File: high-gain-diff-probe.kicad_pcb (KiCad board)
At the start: 4 copper layers, 119.5 x 74.5 mm, 107 parts, among them J1 30V DC IN, J2 BNC, J4 BNC, J5 BNC, K1 FTR-B3SA012Z, K2 FTR-B3SA012Z, Q1 MMBT3906, SW1 MB04L1NCGD, SW2 MB05L1NCGD, SW3 SPDT, SW4 MB04L1NCGD, SW6 SPDT, U1 AD8428BRZ, U2 OP1177AR, U3 BUF634A, U6 LM393, U7 AD8671, U8 BUF634A

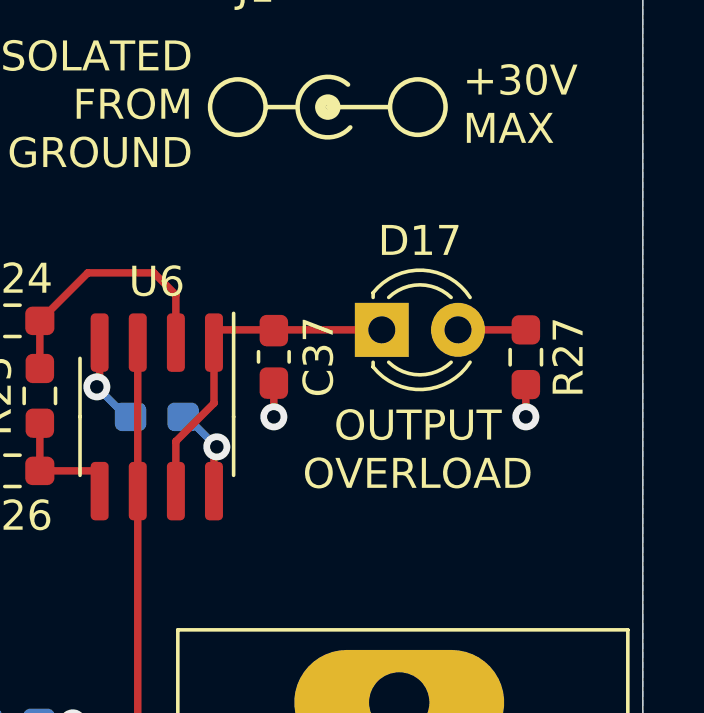
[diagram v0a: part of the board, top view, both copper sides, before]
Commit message: Add MPNs for everything else
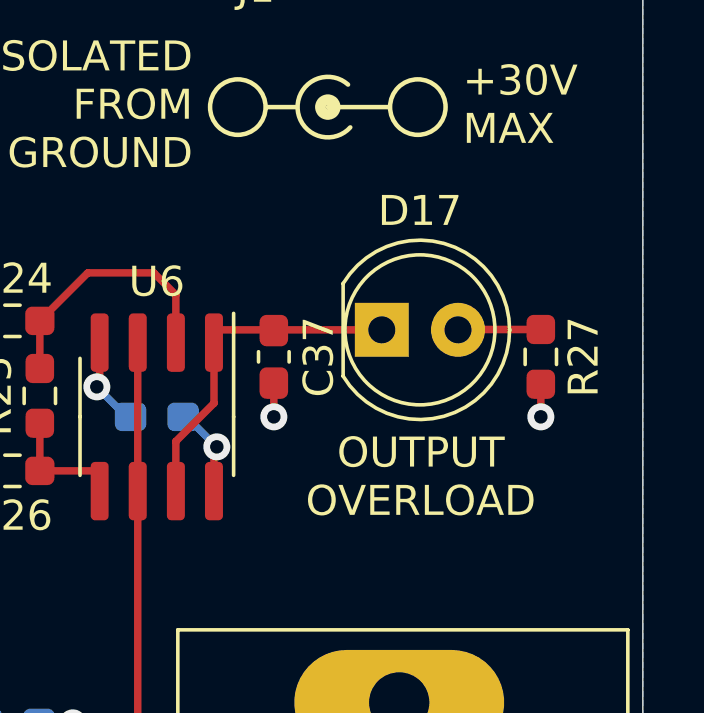
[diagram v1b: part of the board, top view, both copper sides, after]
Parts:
- D17: value LED -> RED LED; footprint LED_THT:LED_D3.0mm -> LED_THT:LED_D5.0mm
- F4: value 1A Fast -> 500mA Fast
- U2: value OP1177AR -> OP1177
- moved R27 0.50 mm to (206.1, 100.9)
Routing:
- net Net-(D17-Pad2): track 2.26 -> 2.77 mm

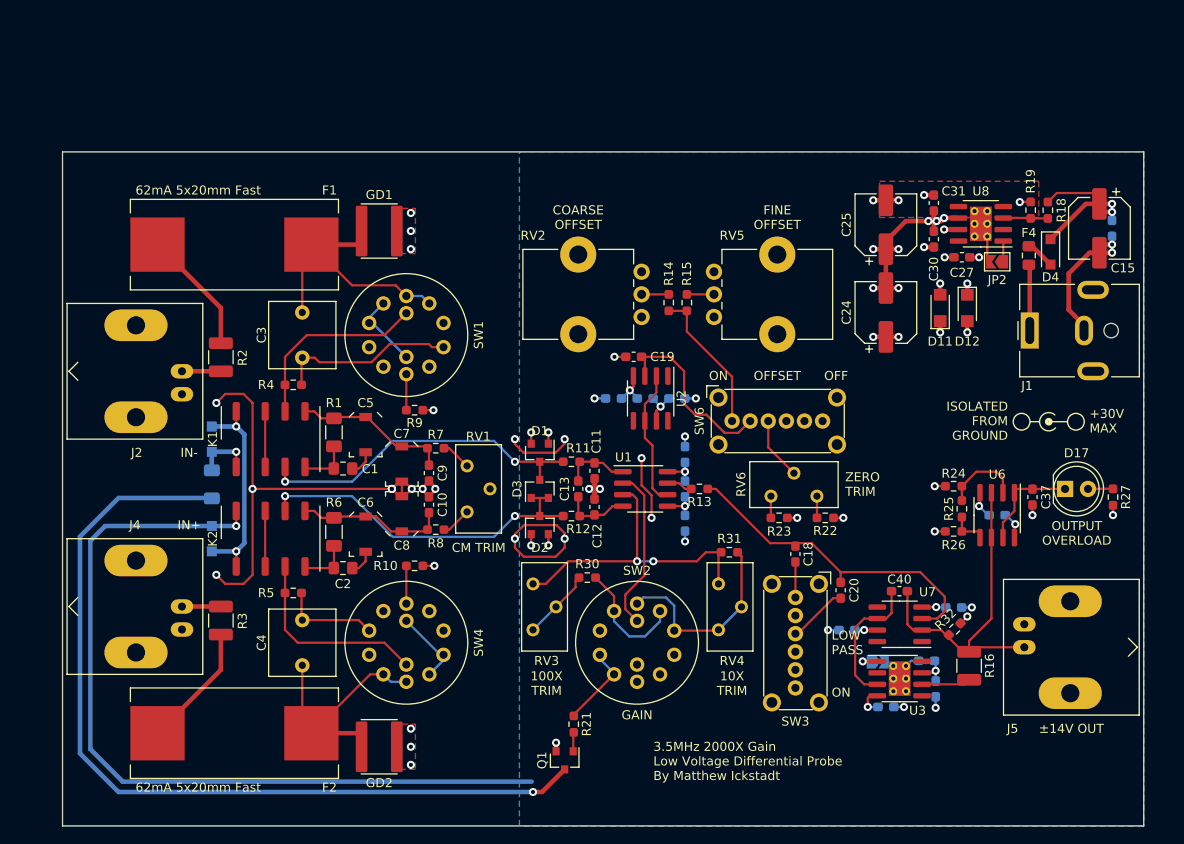
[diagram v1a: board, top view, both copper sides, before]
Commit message: Add mechanical models. Tweak LED Position.
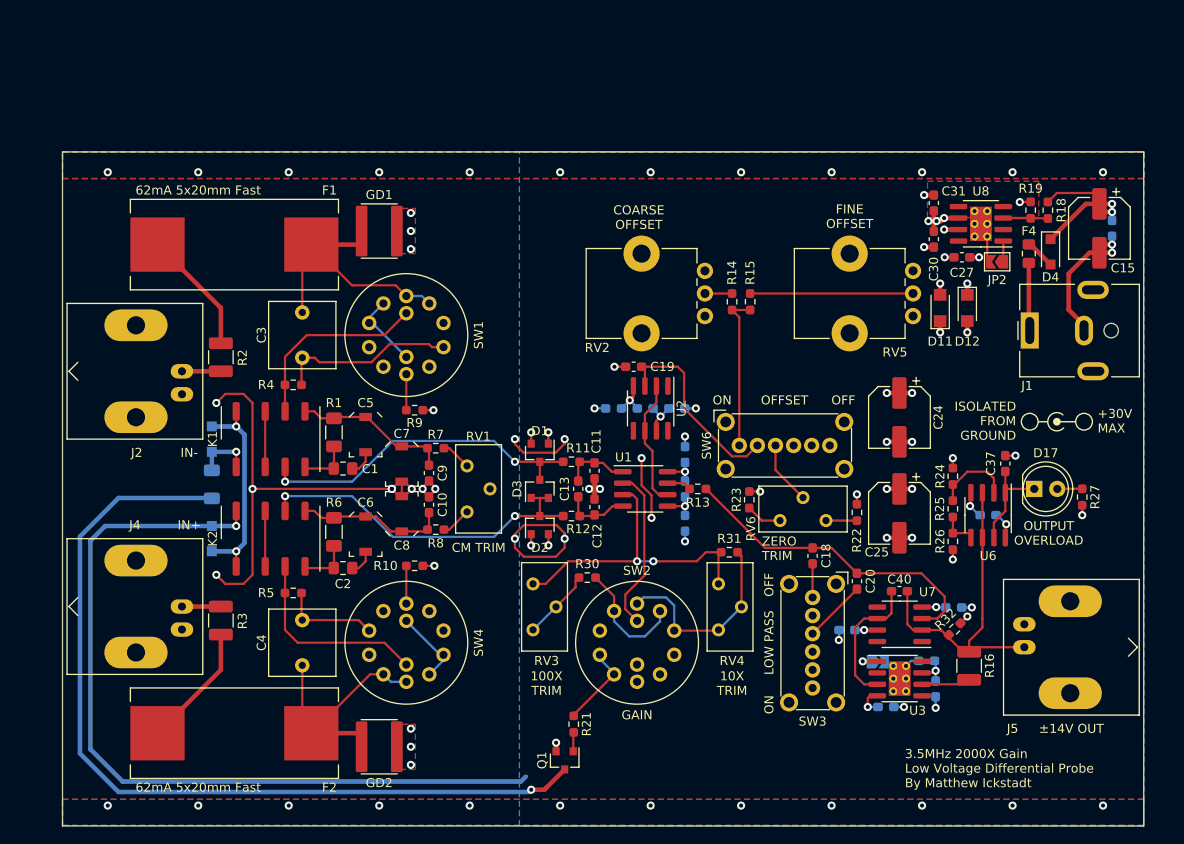
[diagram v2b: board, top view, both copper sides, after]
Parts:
- moved C25 31.9 mm to (182.5, 102.7), turned to 270 degrees
- moved RV5 22.6 mm to (184.0, 75.9), turned to 180 degrees
- moved C24 11.7 mm to (182.5, 92.1), turned to 270 degrees
- moved R14 7.00 mm to (164.0, 79.3)
- moved R15 7.00 mm to (166.0, 79.3)
- moved RV2 7.00 mm to (161.0, 75.9)
- moved C37 4.76 mm to (194.2, 97.2), turned to 270 degrees
- moved R23 3.86 mm to (165.9, 101.2), turned to 90 degrees
- moved R22 3.55 mm to (177.8, 102.6), turned to 270 degrees
- moved D17 3.40 mm to (197.4, 100.0)
- moved R27 3.40 mm to (202.7, 100.9)
- moved RV6 2.88 mm to (169.3, 103.5)
- moved SW6 2.82 mm to (164.8, 95.2)
- moved C20 2.06 mm to (177.8, 110.2)
- moved C18 1.91 mm to (172.9, 107.4)
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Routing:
- net Net-(R15-Pad1): track 3.00 -> 18.0 mm
- net GND: track 195.6 -> 185.6 mm, vias 41 -> 65
- net Net-(R23-Pad1): track 2.41 -> 3.97 mm
- net Net-(C19-Pad2): track 20.8 -> 22.4 mm
- net Net-(C18-Pad1): track 37.0 -> 35.7 mm
- net /REF: track 15.2 -> 14.1 mm
- net Net-(R14-Pad1): track 16.2 -> 17.3 mm
- net Net-(R22-Pad2): track 2.40 -> 3.43 mm
- added copper zone on B.Cu, net GND

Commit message: Tweak layout
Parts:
- D4, D5, D6: footprint Diode_SMD:D_SOD-123F -> Diode_SMD:D_SOD-123
- moved D5 1.40 mm to (107.9, 94.5)
- moved D6 1.40 mm to (107.9, 105.5)
- moved R20 1.40 mm to (107.9, 99.5)
- moved REF** 1.00 mm to (199.9, 91.5)
- moved J1 0.50 mm to (197.4, 82.5)
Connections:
- SW3 pad : GND -> (no net)
- SW6 pad : GND -> (no net)
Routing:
- net Net-(D5-Pad2): track 23.3 -> 21.0 mm
- net ATTEN_EN: track 6.42 -> 5.01 mm
- net Net-(Q1-Pad3): track 96.8 -> 98.1 mm
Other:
- board size 119.5 x 74.5 mm -> 120 x 74.5 mm
- board text added: "Tabs can be filed down to fit snugly into the case tolerance."

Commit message: Update images, gerbers
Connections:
- SW3 pad : (no net) -> GND
- SW6 pad : (no net) -> GND
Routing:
- net GND: track 185.6 -> 193.6 mm
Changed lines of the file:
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@@
     (thickness 1.6)
     (drawings 83)
-    (tracks 661)
+    (tracks 663)
     (zones 0)
     (modules 107)
@@
     (38 B.Mask user)
     (39 F.Mask user)
-    (40 Dwgs.User user)
+    (40 Dwgs.User user hide)
     (41 Cmts.User user)
     (42 Eco1.User user)
@@
     (45 Margin user)
     (46 B.CrtYd user hide)
-    (47 F.CrtYd user)
+    (47 F.CrtYd user hide)
     (48 B.Fab user hide)
     (49 F.Fab user hide)
@@
     (pad 1 thru_hole circle (at 0 0) (size 1.7 1.7) (drill 0.9) (layers *.Cu *.Mask)
       (net 55 "Net-(R14-Pad1)"))
-    (pad "" thru_hole circle (at -1.5 2.6) (size 2 2) (drill 1.2) (layers *.Cu *.Mask))
-    (pad "" thru_hole circle (at 11.6 2.6) (size 2 2) (drill 1.2) (layers *.Cu *.Mask))
-    (pad "" thru_hole circle (at 11.6 -2.6) (size 2 2) (drill 1.2) (layers *.Cu *.Mask))
-    (pad "" thru_hole circle (at -1.5 -2.6) (size 2 2) (drill 1.2) (layers *.Cu *.Mask))
+    (pad "" thru_hole circle (at -1.5 2.6) (size 2 2) (drill 1.2) (layers *.Cu *.Mask)
+      (net 1 GND))
+    (pad "" thru_hole circle (at 11.6 2.6) (size 2 2) (drill 1.2) (layers *.Cu *.Mask)
+      (net 1 GND))
+    (pad "" thru_hole circle (at 11.6 -2.6) (size 2 2) (drill 1.2) (layers *.Cu *.Mask)
+      (net 1 GND))
+    (pad "" thru_hole circle (at -1.5 -2.6) (size 2 2) (drill 1.2) (layers *.Cu *.Mask)
+      (net 1 GND))
     (model ${KIPRJMOD}/3DModel/c-1825263-2-a-3d.igs
       (offset (xyz 5 0 10.1))
@@
     (pad 1 thru_hole circle (at 0 0 270) (size 1.7 1.7) (drill 0.9) (layers *.Cu *.Mask)
       (net 12 "Net-(C18-Pad2)"))
-    (pad "" thru_hole circle (at -1.5 2.6 270) (size 2 2) (drill 1.2) (layers *.Cu *.Mask))
-    (pad "" thru_hole circle (at 11.6 2.6 270) (size 2 2) (drill 1.2) (layers *.Cu *.Mask))
-    (pad "" thru_hole circle (at 11.6 -2.6 270) (size 2 2) (drill 1.2) (layers *.Cu *.Mask))
-    (pad "" thru_hole circle (at -1.5 -2.6 270) (size 2 2) (drill 1.2) (layers *.Cu *.Mask))
+    (pad "" thru_hole circle (at -1.5 2.6 270) (size 2 2) (drill 1.2) (layers *.Cu *.Mask)
+      (net 1 GND))
+    (pad "" thru_hole circle (at 11.6 2.6 270) (size 2 2) (drill 1.2) (layers *.Cu *.Mask)
+      (net 1 GND))
+    (pad "" thru_hole circle (at 11.6 -2.6 270) (size 2 2) (drill 1.2) (layers *.Cu *.Mask)
+      (net 1 GND))
+    (pad "" thru_hole circle (at -1.5 -2.6 270) (size 2 2) (drill 1.2) (layers *.Cu *.Mask)
+      (net 1 GND))
     (model ${KIPRJMOD}/3DModel/c-1825263-2-a-3d.igs
       (offset (xyz 5 0 10.1))
@@
   (segment (start 144.6 104) (end 141 104) (width 0.25) (layer F.Cu) (net 0))
   (segment (start 144.6 104) (end 145.5 104.9) (width 0.25) (layer F.Cu) (net 0))
+  (segment (start 118.1 113.9) (end 118.1 117.5) (width 0.25) (layer In1.Cu) (net 1))
+  (segment (start 118 86.6) (end 118 82.2) (width 0.25) (layer In1.Cu) (net 1))
   (via (at 95 135) (size 0.9) (drill 0.45) (layers F.Cu B.Cu) (net 1))
   (via (at 105 135) (size 0.9) (drill 0.45) (layers F.Cu B.Cu) (net 1))
@@
   (segment (start 115.4 110.2) (end 113.8 110.2) (width 0.25) (layer In1.Cu) (net 1))
   (segment (start 115.4 89.7) (end 113.8 89.7) (width 0.25) (layer In1.Cu) (net 1))
-  (segment (start 120.2 113.8) (end 120.2 117.6) (width 0.25) (layer In1.Cu) (net 1))
+  (segment (start 122.4 113.9) (end 122.4 117.7) (width 0.25) (layer In1.Cu) (net 1))
   (segment (start 123.2 120.5) (end 124 121.3) (width 0.25) (layer In1.Cu) (net 1))
   (segment (start 120.6 123.2) (end 121.3 123.9) (width 0.25) (layer In1.Cu) (net 1))
@@
   (segment (start 122 76.2) (end 120.8 77.4) (width 0.25) (layer In1.Cu) (net 1))
   (segment (start 117.2 77.6) (end 115.8 77.6) (width 0.25) (layer In1.Cu) (net 1))
-  (segment (start 120 82) (end 120 86.8) (width 0.25) (layer In1.Cu) (net 1))
+  (segment (start 121.5 82) (end 121.5 86.8) (width 0.25) (layer In1.Cu) (net 1))
   (via (at 128.5 71.5) (size 0.9) (drill 0.45) (layers F.Cu B.Cu) (net 1))
   (via (at 128.5 73.5) (size 0.9) (drill 0.45) (layers F.Cu B.Cu) (net 1))
@@
     (polygon
       (pts
-        (xy 209.5 137.25) (xy 90 137.25) (xy 90 62.75) (xy 209.5 62.75)
+        (xy 209.5 137.25) (xy 90.5 137.25) (xy 90.5 62.75) (xy 209.5 62.75)
       )
     )

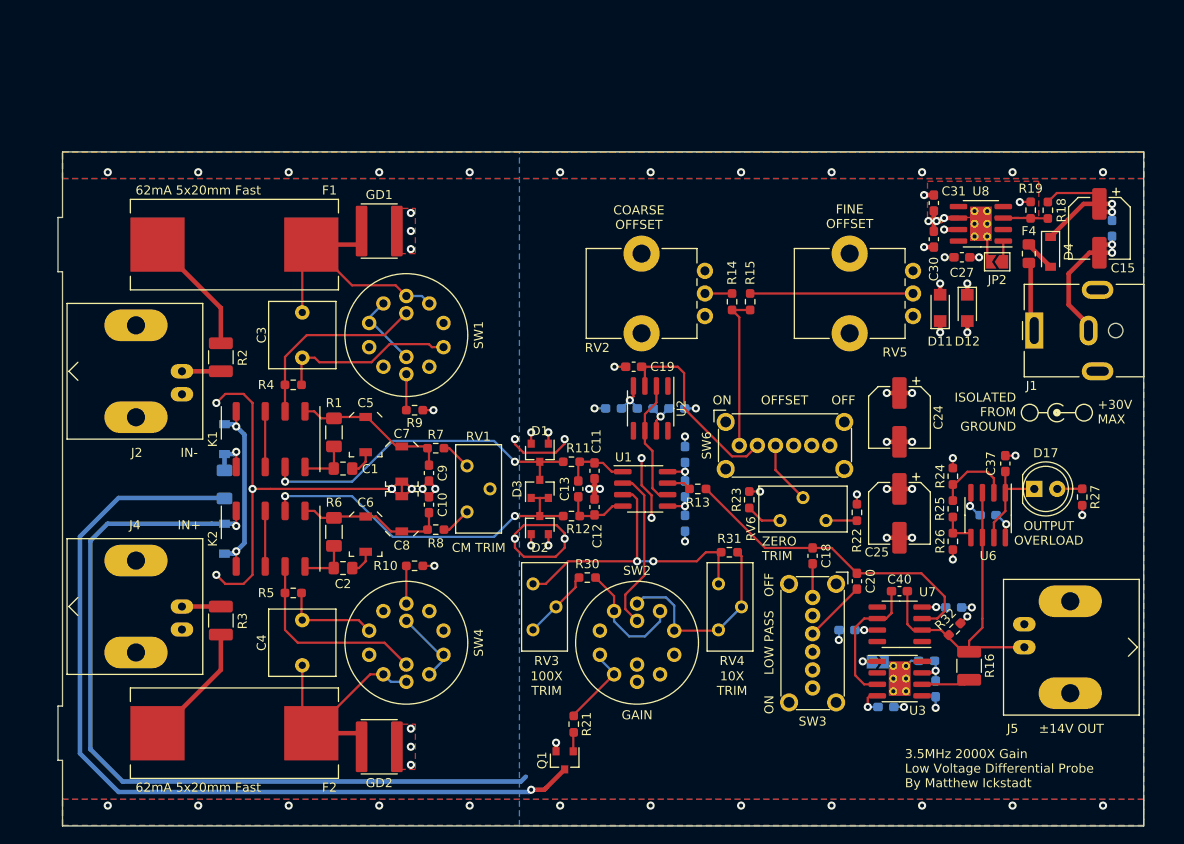
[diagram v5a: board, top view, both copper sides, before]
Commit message: Begin work on new version with no relays and manual attenuator switching
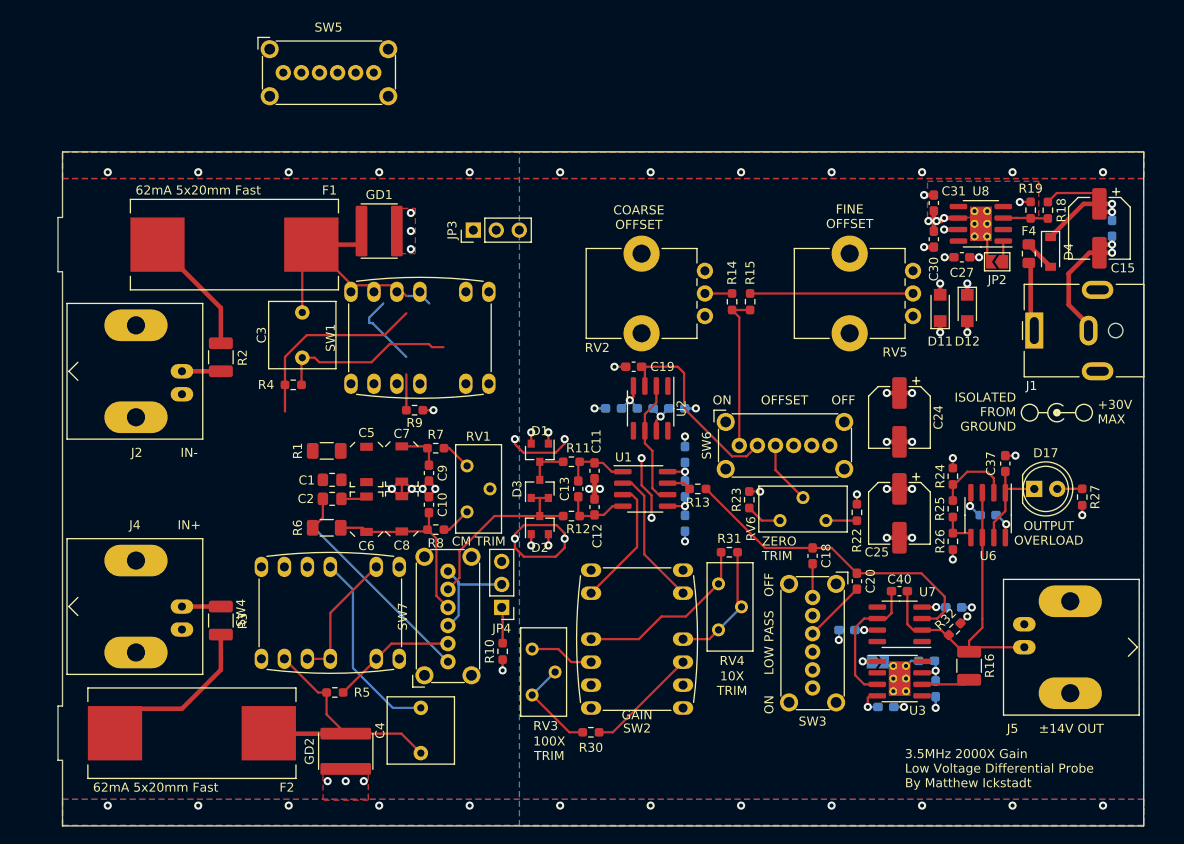
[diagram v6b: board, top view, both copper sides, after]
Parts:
- removed D5, D6: DSS15, Diode_SMD:D_SOD-123
- removed K1, K2: FTR-B3SA012Z, Relay_SMD:Relay_Fujitsu_FTR-B3S
- removed Q1: MMBT3906, Package_TO_SOT_SMD:SOT-23
- removed R20: 1k 1/4W, Resistor_SMD:R_1206_3216Metric_Pad1.30x1.75mm_HandSolder
- removed R21: 100k, Resistor_SMD:R_0603_1608Metric_Pad0.98x0.95mm_HandSolder
- added JP3: TERM, Connector_PinHeader_2.54mm:PinHeader_1x03_P2.54mm_Vertical, F.Cu at (135.4, 71.4)
- added JP4: TERM, Connector_PinHeader_2.54mm:PinHeader_1x03_P2.54mm_Vertical, F.Cu at (138.5, 113.1)
- added SW5: DP3T, high-gain-diff-probe:SW_TE_1825263-2_DPDT, F.Cu at (114.4, 54.0)
- added SW7: DP3T, high-gain-diff-probe:SW_TE_1825263-2_DPDT, F.Cu at (132.6, 119.1)
- C3, C4: value 1uF 100V FILM -> 1uF 100V
- SW1, SW4: value MB04L1NCGD -> DP3T; footprint high-gain-diff-probe:SW_DPNT_CK_M -> high-gain-diff-probe:SW_NKK_MRB24B
- SW2: value MB05L1NCGD -> DP3T; footprint high-gain-diff-probe:SW_DPNT_CK_M -> high-gain-diff-probe:SW_NKK_MRB24B
- moved R30 17.1 mm to (148.4, 126.9)
- moved C4 16.3 mm to (129.6, 124.2)
- moved R10 13.6 mm to (138.6, 118.0), turned to 90 degrees
- moved R5 11.9 mm to (120.1, 122.5), turned to 0 degrees
- moved SW4 9.02 mm to (119.6, 113.7)
- moved C2 7.74 mm to (119.8, 101.1)
- moved RV3 7.20 mm to (141.9, 117.7)
- moved F2 4.70 mm to (104.3, 127.0)
- moved GD2 3.73 mm to (121.3, 129.0), turned to 270 degrees
- moved C5 3.30 mm to (123.6, 97.3)
- moved C6 2.20 mm to (123.6, 102.8), turned to 90 degrees
- moved R1 2.20 mm to (119.2, 95.8), turned to 180 degrees
- moved C1 1.73 mm to (119.8, 99.0)
- moved SW1 1.53 mm to (129.5, 83.3)
- moved R6 0.92 mm to (119.2, 104.3), turned to 180 degrees
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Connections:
- net ATTEN+ renamed /ATTEN+
- net ATTEN- renamed /ATTEN-
- R10 pad 1: Net-(R10-Pad1) -> GND
- R10 pad 2: GND -> Net-(JP4-Pad1)
- R31 pad 1: /FIL+ -> Net-(R31-Pad1)
- R4 pad 1: Net-(C3-Pad1) -> Net-(C3-Pad2)
- R4 pad 2: Net-(K1-Pad6) -> Net-(R4-Pad2)
- R5 pad 1: Net-(C4-Pad1) -> Net-(C4-Pad2)
- R5 pad 2: Net-(K2-Pad3) -> Net-(R5-Pad2)
- R9 pad 1: Net-(R9-Pad1) -> Net-(JP3-Pad2)
- RV3 pad 1: /FIL+ -> Net-(RV3-Pad1)
- RV4 pad 1: /FIL+ -> Net-(R31-Pad1)
- SW1 pad 1: Net-(SW1-Pad1) -> (no net)
- SW1 pad 2: Net-(SW1-Pad1) -> GND
- SW1 pad 3: Net-(C3-Pad2) -> Net-(C3-Pad1)
- SW1 pad 5: (no net) -> Net-(SW1-Pad5)
- SW1 pad 6: Net-(C3-Pad1) -> Net-(SW1-Pad5)
- SW2 pad 2: /RG_100X -> Net-(RV3-Pad1)
- SW2 pad 3: /RG_10X -> Net-(R31-Pad1)
- SW2 pad 4: /RG_100X -> (no net)
- SW2 pad 5: /RG_10X -> /RG_100X
- SW2 pad 6: GND -> /RG_10X
- SW3 pad : GND -> (no net)
- SW4 pad 1: Net-(C4-Pad1) -> (no net)
- SW4 pad 3: Net-(R10-Pad1) -> Net-(C4-Pad1)
- SW4 pad 4: (no net) -> Net-(C4-Pad2)
- SW4 pad 5: (no net) -> Net-(SW4-Pad5)
- SW4 pad 6: Net-(SW4-Pad6) -> Net-(SW4-Pad5)
- SW6 pad : GND -> (no net)
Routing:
- net Net-(Q1-Pad3): track 98.1 -> 0.00 mm, vias 1 -> 0
- net GND: track 193.6 -> 98.8 mm, vias 65 -> 61
- net -15V: track 145.9 -> 54.2 mm, vias 19 -> 18
- net /ATTEN-: track 37.2 -> 4.59 mm, vias 2 -> 0
- net Net-(K2-Pad3): track 22.0 -> 0.00 mm
- net Net-(R4-Pad2): track 0.00 -> 21.4 mm
- net Net-(K1-Pad6): track 21.4 -> 0.00 mm
- net Net-(D5-Pad2): track 21.0 -> 0.00 mm, vias 2 -> 0
- net /FIL+: track 34.5 -> 14.2 mm, vias 2 -> 0
- net Net-(R31-Pad1): track 0.00 -> 20.2 mm
- net Net-(C2-Pad2): track 5.71 -> 24.4 mm
- net /ATTEN+: track 39.1 -> 21.7 mm, vias 2 -> 0
- net Net-(SW4-Pad5): track 0.00 -> 14.8 mm
- net Net-(R5-Pad2): track 0.00 -> 13.9 mm
- net Net-(C5-Pad1): track 17.3 -> 4.86 mm
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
